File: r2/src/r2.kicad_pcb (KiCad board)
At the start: 4 copper layers, 110.2 x 145.8 mm, 234 parts, among them J1 532610271, J10 PJ-320D, J2 USB-C-12, J3 UJ2-AH-1-SMT, J4 TF-15x15, J5 AFC07-S24ECA-00, J6 DNP, J7 2x03-socket-2.54-through-board, J8 DNP, J9 532610271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

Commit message: PCB sent for fabrication. Move all names and values to Degs.User layer so we can exclude from assembly drawings
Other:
- board text added: "credits: badge.team norbert dr kl jim rgilton nick mareen celina"
- board text removed: "credits: badge.team norbert dr kl jim rgilton nick celina"

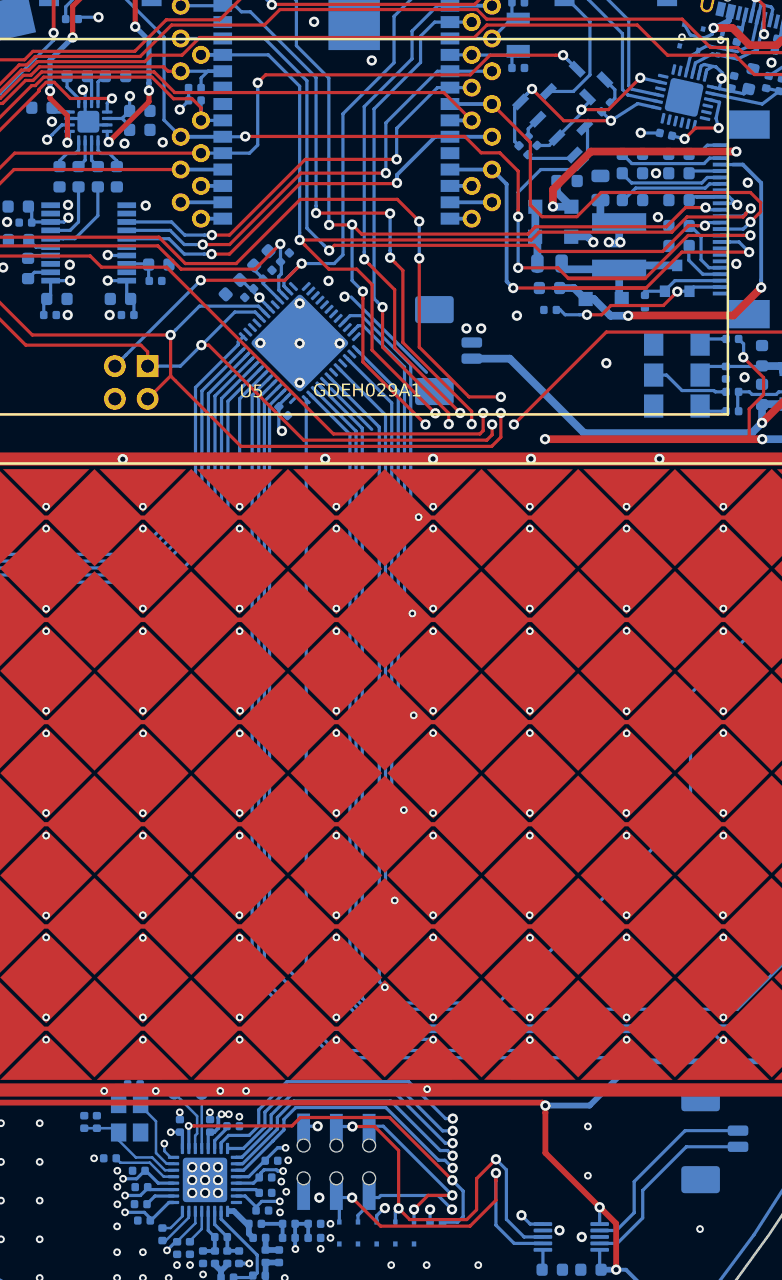
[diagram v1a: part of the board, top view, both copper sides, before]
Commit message: Replace D1, D2, D4 to include diode direction marker for assembly drawing
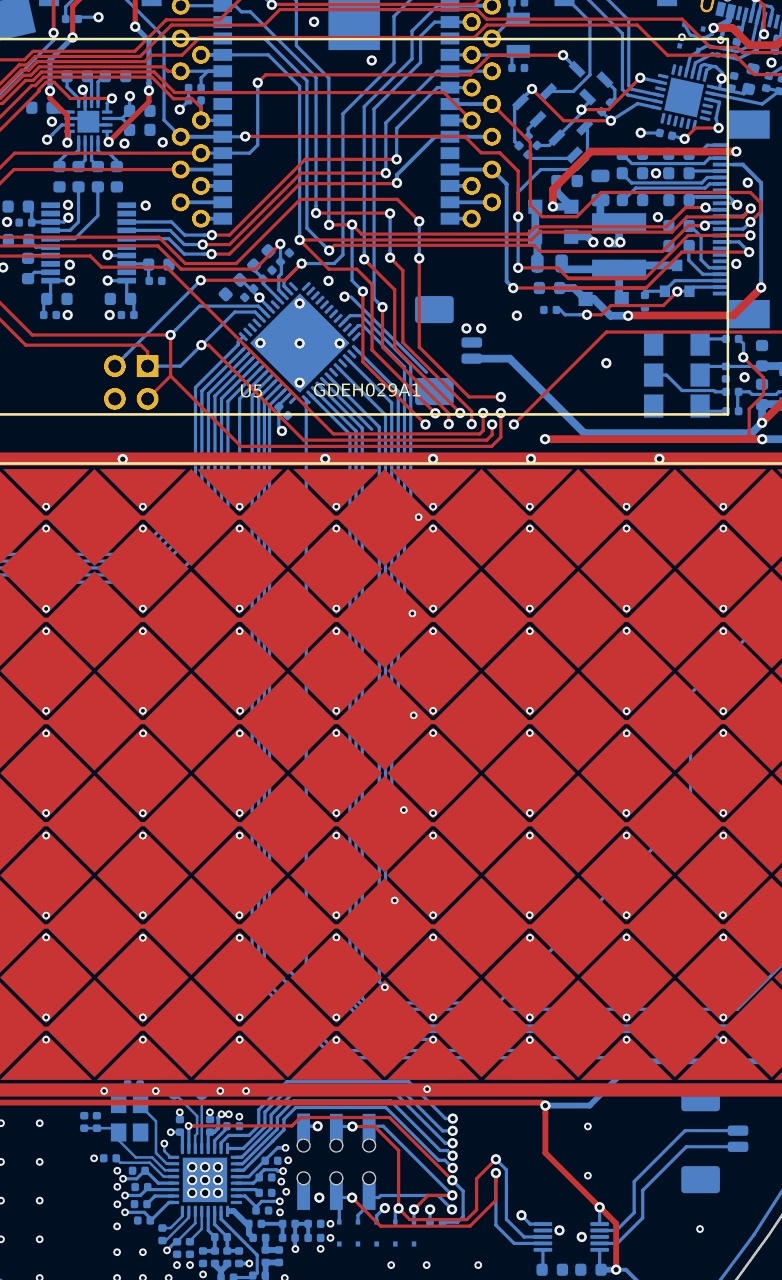
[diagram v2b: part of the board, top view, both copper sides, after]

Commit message: Noise
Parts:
- D1, D2, D4: footprint digikey-footprints:1206 -> jeffmakes-footprints:D-1206
- J3: value UJ2-AH-1-SMT -> USB-A-10mm-flangeless
